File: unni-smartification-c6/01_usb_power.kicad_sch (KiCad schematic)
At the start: 38 parts, among them J1 USB-C (replacement daughterbo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, J2 Li-Ion 1S JST-PH, J3 UNNI AC / 5V input, J4 UNNI DC / battery input, Q1 AO3401A, Q2 AO3401A, Q3 AO3400A, Q4 AO3400A, Q5 AO3400A charge enable, U1 MCP73831T-2ACI/OT, U2 TPS63031DSK, U3 TPS613222ADBZ (5V)

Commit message: iteration on schematics and simulation
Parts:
- removed Q5: AO3400A charge enable, Package_TO_SOT_SMD:SOT-23, symbol Transistor_FET:Q_NMOS_GSD
- removed R4: 100k, Resistor_SMD:R_0603_1608Metric, symbol Device:R
- added R13: 1M, Resistor_SMD:R_0603_1608Metric, symbol Device:R
- R9: value 100k -> 1M
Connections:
- net GND: now also R3.2, R6.1, R13.1; no longer R6.2
- net VBUS: now also R13.2; no longer C3.1, C4.1, D1.1 (K), Q1.2 (S), U2.5 (VIN), U2.6 (EN), U2.8 (VINA)
- net at Q1.1 (G), R5.2: now also R6.2; no longer R6.1
- new net SYS: C3.1, C4.1, D1.1 (K), Q1.2 (S), U2.5 (VIN), U2.6 (EN), U2.8 (VINA)
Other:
- note added: "MCP73831 runs autonomously: R3 = 3.3 kΩ sets ~300 mA; STAT is monitored by the ESP. Battery NTC remains firmware-supervised."
- moved on the sheet: C1, C7, C8, C9, D2, D3, D4, L2, Q1, Q3, R1, R2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

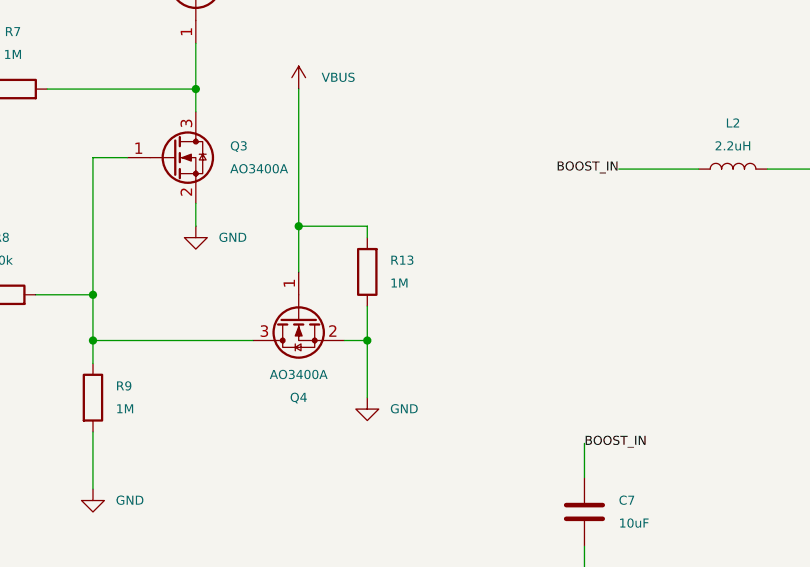
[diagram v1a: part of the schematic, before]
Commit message: Validate power paths and fix KiCad SPICE models
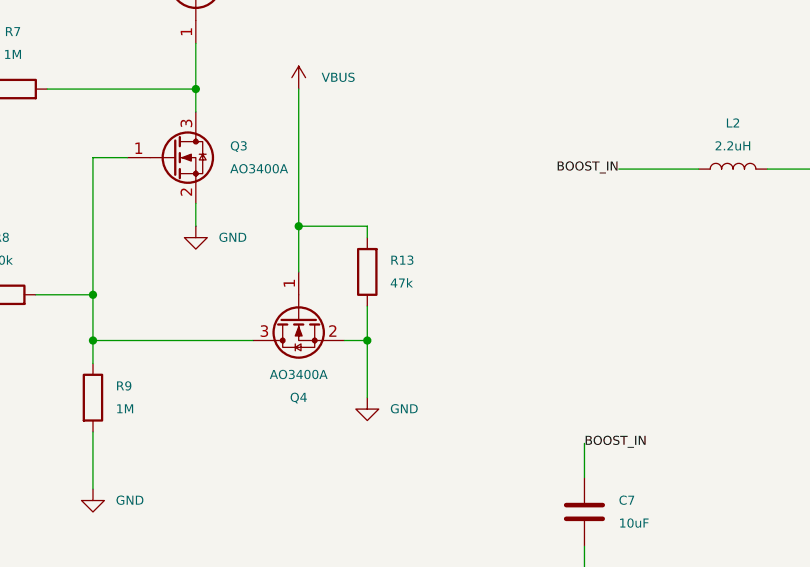
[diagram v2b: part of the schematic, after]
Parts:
- R13: value 1M -> 47k
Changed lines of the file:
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@@
 		(title "USB + Power")
 		(date "2026-08-19")
-		(rev "A-v28-final")
+		(rev "A-v29-validated")
 		(company "Unni CO2 Smartification")
 	)
@@
 			)
 		)
-		(property "Value" "1M"
+		(property "Value" "47k"
 			(at 72.39 186.69 0)
 			(show_name no)

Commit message: further iterations
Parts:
- R1, R11, R12, R13, R2, R3, R5, R6, R7, R8, R9: footprint Resistor_SMD:R_0603_1608Metric -> Resistor_SMD:R_0805_2012Metric_Pad1.20x1.40mm_HandSolder
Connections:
- net +BATT: now also R7.2; no longer R7.1
- net at Q2.1 (G), Q3.3 (D): now also R7.1; no longer R7.2
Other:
- moved on the sheet: C1, C2, C3, C4, C5, C6, C7, C8, C9, D3, D4, L1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

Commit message: first try doing a pcb with kicad 10.99
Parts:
- removed J3: UNNI AC / 5V input, Connector_JST:JST_XH_B2B-XH-A_1x02_P2.50mm_Vertical, symbol Connector_Generic:Conn_01x02
- D2: now left out of the parts list
- J2: footprint Connector_JST:JST_PH_B2B-PH-K_1x02_P2.00mm_Vertical -> Connector_JST:JST_PH_S2B-PH-K_1x02_P2.00mm_Horizontal
- J4: value UNNI DC / battery input -> UNNI DC / battery input - AC / 5V Input; footprint Connector_JST:JST_XH_B2B-XH-A_1x02_P2.50mm_Vertical -> Connector_JST:JST_XH_S3B-XH-A_1x03_P2.50mm_Horizontal; symbol Connector_Generic:Conn_01x02 -> Connector_Generic:Conn_01x03
- L1, L2: footprint Inductor_SMD:L_3.2x2.5_H1.2 -> Inductor_SMD:L_TDK_NLV32_3.2x2.5mm
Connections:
- net GND: now also J4.3 (Pin_3); no longer J4.2 (Pin_2)
- net UNNI_AC: now also J4.2 (Pin_2)
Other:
- moved on the sheet: C9, D3, D4, J2

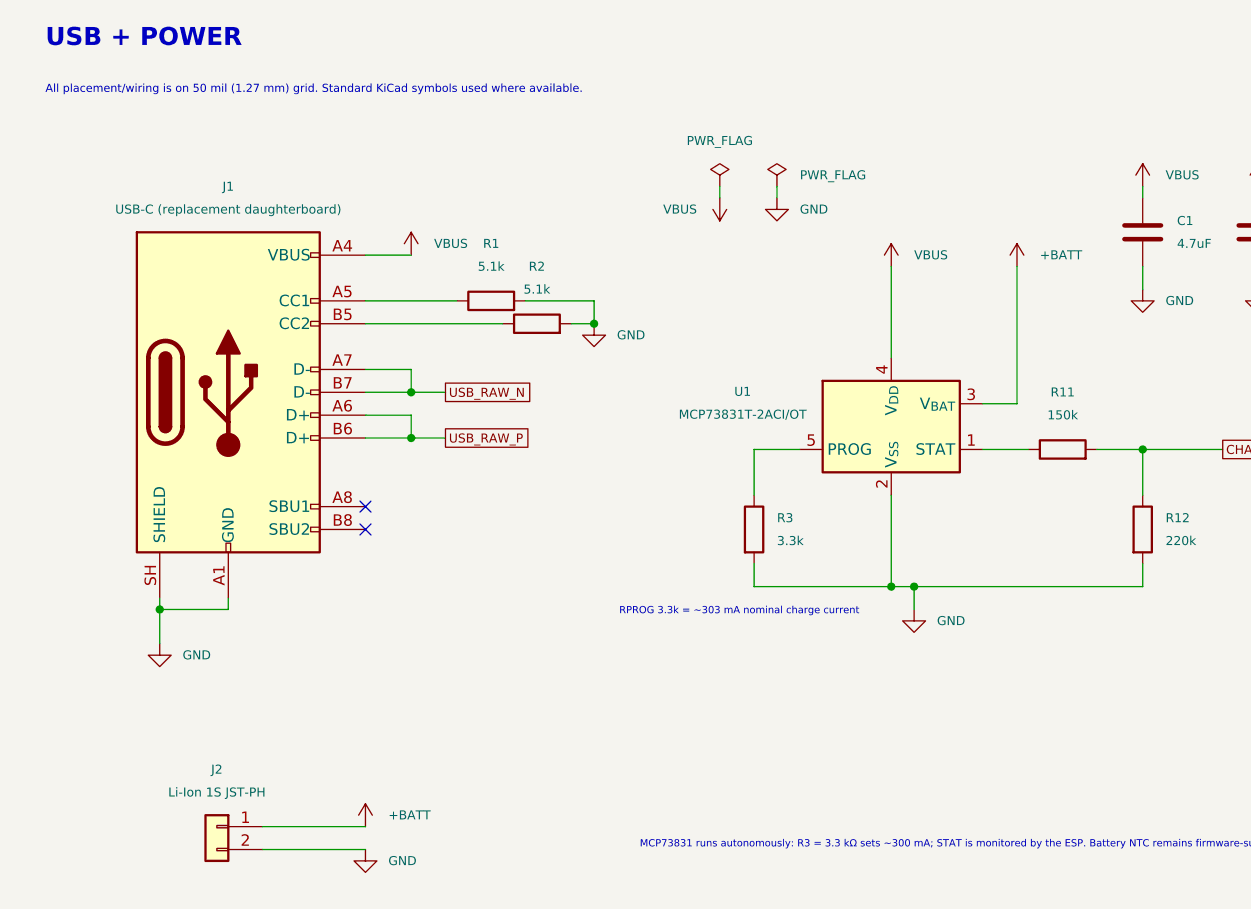
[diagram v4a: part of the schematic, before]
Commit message: Fix PCB net mapping and validate against schematic
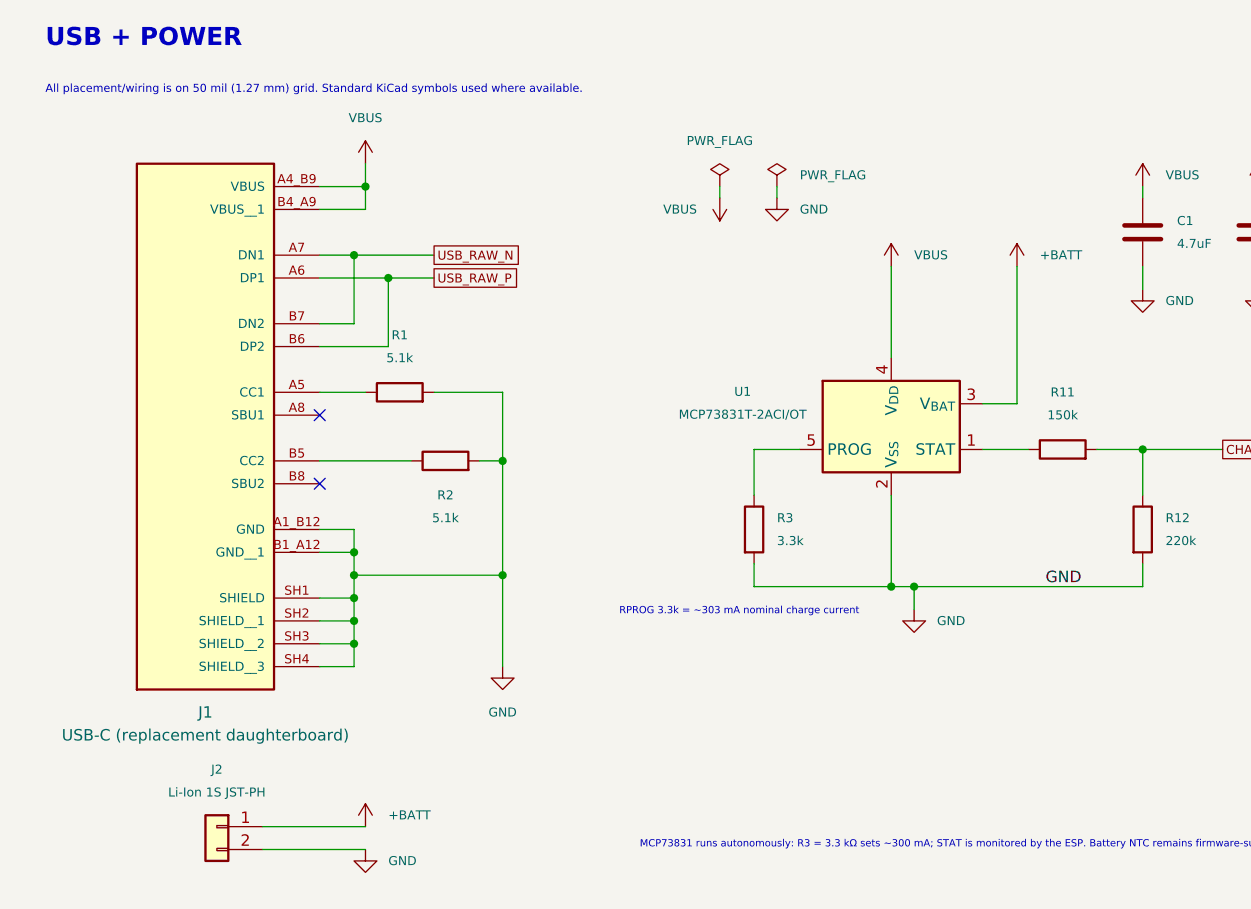
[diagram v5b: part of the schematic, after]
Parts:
- removed J1: USB-C (replacement daughterboard), Connector_USB:USB_C_Receptacle_GCT_USB4105-xx-A_16P_TopMnt_Horizontal, symbol Connector:USB_C_Receptacle_USB2.0_16P
- added J1: USB-C (replacement daughterboard), Misc:SAMESKY_UJ20-C-H-G-SMT-1-P16-TR, symbol Misc:UJ20-C-H-G-SMT-1-P16-TR
- C1, C2, C3, C5, C6, C7, C8: footprint Capacitor_SMD:C_0805_2012Metric -> Capacitor_SMD:C_0805_2012Metric_Pad1.18x1.45mm_HandSolder
- C4, C9: footprint Capacitor_SMD:C_0603_1608Metric -> Capacitor_SMD:C_0603_1608Metric_Pad1.08x0.95mm_HandSolder
- J2: footprint Connector_JST:JST_PH_S2B-PH-K_1x02_P2.00mm_Horizontal -> Connector_JST:JST_PH_S2B-PH-SM4-TB_1x02-1MP_P2.00mm_Horizontal
- J4: footprint Connector_JST:JST_XH_S3B-XH-A_1x03_P2.50mm_Horizontal -> Connector_JST:JST_PH_S3B-PH-SM4-TB_1x03-1MP_P2.00mm_Horizontal
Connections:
- net GND: now also J1.A1_B12 (GND), J1.B1_A12 (GND__1), J1.SH1 (SHIELD), J1.SH2 (SHIELD__1), J1.SH3 (SHIELD__2), J1.SH4 (SHIELD__3)
- net USB_RAW_N: now also J1.A7 (DN1), J1.B7 (DN2)
- net USB_RAW_P: now also J1.A6 (DP1), J1.B6 (DP2)
- net VBUS: now also J1.A4_B9 (VBUS), J1.B4_A9 (VBUS__1)
- net at R1.1: now also J1.A5 (CC1)
- net at R2.1: now also J1.B5 (CC2)
